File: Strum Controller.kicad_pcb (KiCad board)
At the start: 2 copper layers, 18 parts, among them J1 USB_C_Receptacle_USB2.0, U1 RP2040, U2 NCP1117-3.3_SOT223

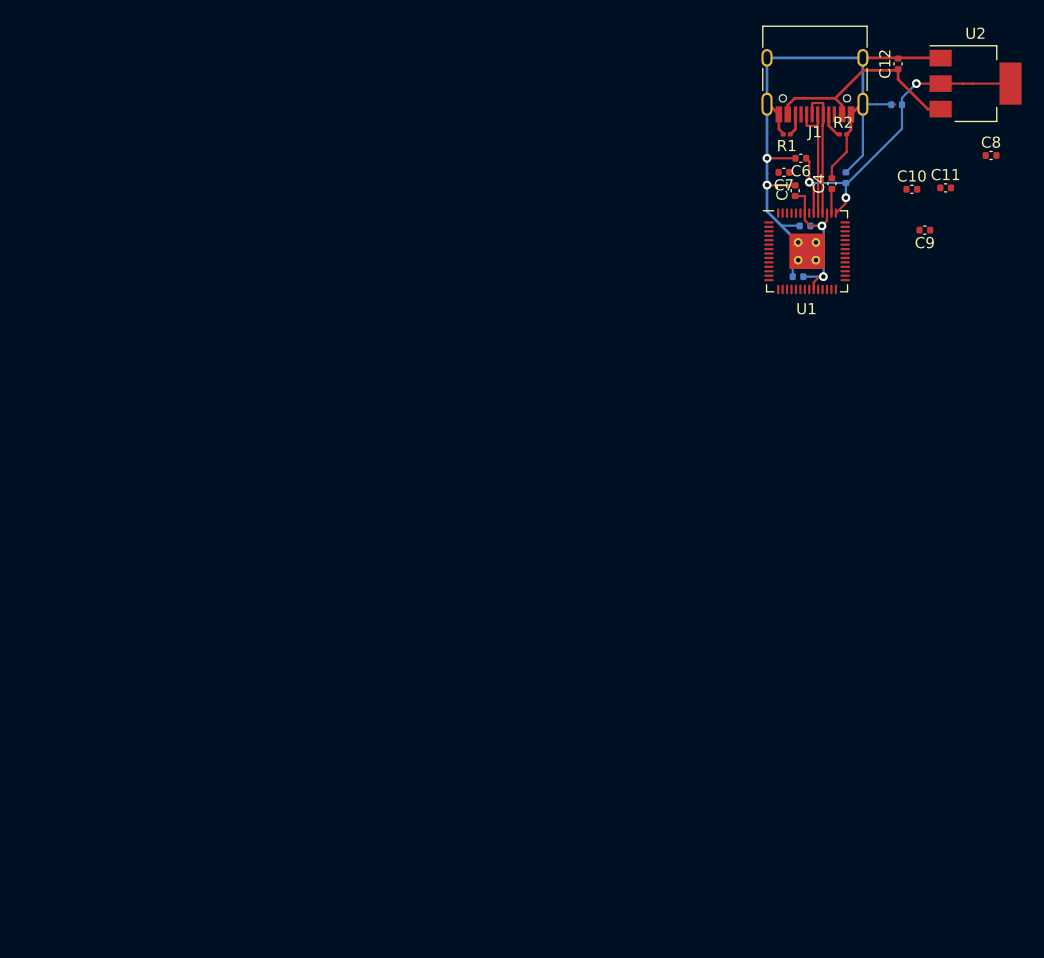
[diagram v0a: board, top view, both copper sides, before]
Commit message: Restart design using modified RP2040 minimal design from RasPi Foundation
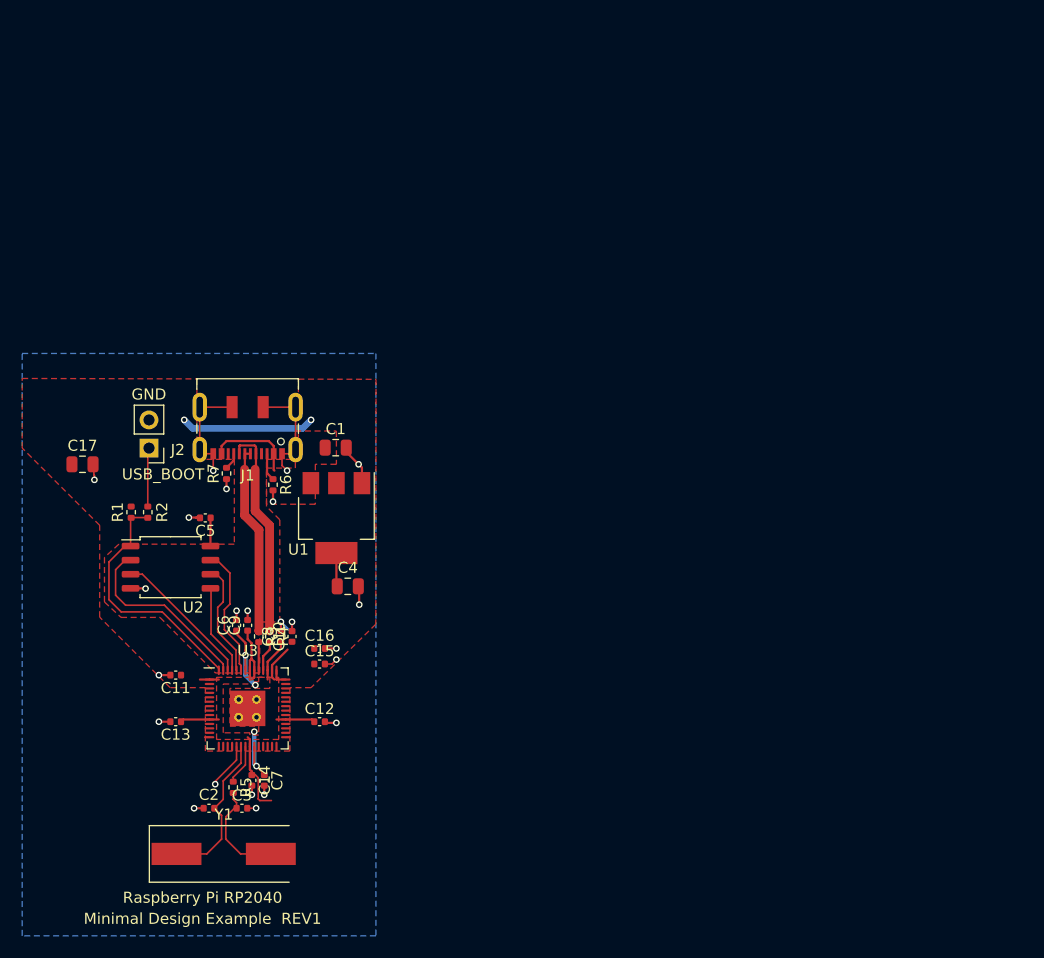
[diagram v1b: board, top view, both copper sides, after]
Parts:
- added C14: 100n, Capacitor_SMD:C_0402_1005Metric, F.Cu at (100.4, 106.5)
- added C15: 100n, Capacitor_SMD:C_0402_1005Metric, F.Cu at (106.5, 96.0)
- added C16: 100n, Capacitor_SMD:C_0402_1005Metric, F.Cu at (106.5, 94.6)
- added C17: 10u, Capacitor_SMD:C_0805_2012Metric, F.Cu at (85.1, 78.0)
- added J2: Conn_01x02, Connector_PinHeader_2.54mm:PinHeader_1x02_P2.54mm_Vertical, F.Cu at (91.1, 76.5)
- added R3: 27, Resistor_SMD:R_0402_1005Metric, F.Cu at (101.0, 93.5)
- added R4: 27, Resistor_SMD:R_0402_1005Metric, F.Cu at (102.0, 93.5)
- added R5: 1k, Resistor_SMD:R_0402_1005Metric, F.Cu at (98.7, 107.1)
- added R6: 5k1, Resistor_SMD:R_0402_1005Metric, F.Cu at (102.3, 79.8)
- added R7: 5k1, Resistor_SMD:R_0402_1005Metric, F.Cu at (98.1, 78.8)
- added U3: RP2040, kicad-rp2040:RP2040_QFN-56_EP_7x7_Pitch0.4mm_ThermalVias, F.Cu at (100.0, 100.0)
- added Y1: ABLS-12.000MHZ-B4-T, Crystal:Crystal_SMD_HC49-SD, F.Cu at (97.8, 113.1)
- C1, C4: value 100n -> 10u; footprint Capacitor_SMD:C_0402_1005Metric -> Capacitor_SMD:C_0805_2012Metric
- C10, C8: value 100n -> 1u
- C12: value 10u -> 100n
- C13: value 10u -> 100n; moved to F.Cu
- C2: value 100n -> 27p; moved to F.Cu
- C3: value 1u -> 27p; moved to F.Cu
- C5: value 1u -> 100n; moved to F.Cu
- J1: footprint Connector_USB:USB_C_Receptacle_HRO_TYPE-C-31-M-12 -> Connector_USB:USB_C_Receptacle_JAE_DX07S016JA1R1500
- R1: value 5k1 -> 1k; footprint Resistor_SMD:R_0201_0603Metric -> Resistor_SMD:R_0402_1005Metric
- R2: value 5k1 -> DNF; footprint Resistor_SMD:R_0201_0603Metric -> Resistor_SMD:R_0402_1005Metric
- U1: value RP2040 -> NCP1117-3.3_SOT223; footprint kicad-rp2040:RP2040_QFN-56_EP_7x7_Pitch0.4mm_ThermalVias -> Package_TO_SOT_SMD:SOT-223-3_TabPin2
- U2: value NCP1117-3.3_SOT223 -> W25Q128JVS; footprint Package_TO_SOT_SMD:SOT-223-3_TabPin2 -> Package_SO:SOIC-8_5.275x5.275mm_P1.27mm
- moved C13 85.5 mm to (93.5, 101.2)
- moved U2 84.6 mm to (93.0, 87.3)
- moved C11 82.1 mm to (93.5, 97.0), turned to 180 degrees
- moved C12 79.0 mm to (106.5, 101.2), turned to 0 degrees
- moved C8 77.3 mm to (103.0, 93.5), turned to 90 degrees
- moved C3 73.0 mm to (99.5, 109.0), turned to 0 degrees
- moved R2 72.6 mm to (89.5, 82.3), turned to -90 degrees
- moved C7 72.1 mm to (101.5, 106.5), turned to -90 degrees
- moved C2 71.5 mm to (96.5, 109.0)
- moved C9 70.7 mm to (100.0, 92.5), turned to 90 degrees
- moved C10 68.9 mm to (104.0, 93.5), turned to 90 degrees
- moved R1 66.9 mm to (91.0, 82.3), turned to 90 degrees
- moved C6 66.0 mm to (99.0, 92.5), turned to 90 degrees
- moved C5 65.4 mm to (96.2, 82.8), turned to 180 degrees
- moved J1 60.1 mm to (100.0, 74.0)
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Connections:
- C1 pad 1: +1V1 -> VBUS
- C12 pad 1: VBUS -> +3V3
- C2 pad 1: +1V1 -> /XIN
- C3 pad 1: +1V1 -> Net-(C3-Pad1)
- C6 pad 1: +3V3 -> +1V1
- C7 pad 1: +3V3 -> +1V1
- C8 pad 1: +3V3 -> +1V1
- J1 pad A6: /USB_+ -> /USB_D+
- J1 pad A7: /USB_- -> /USB_D-
- J1 pad B6: /USB_+ -> /USB_D+
- J1 pad B7: /USB_- -> /USB_D-
- R1 pad 1: Net-(J1-PadB5) -> /QSPI_SS
- R1 pad 2: GND -> /~{USB_BOOT}
- R2 pad 1: Net-(J1-PadA5) -> +3V3
- R2 pad 2: GND -> /QSPI_SS
- U1 pad 1: +3V3 -> GND
- U1 pad 2: unconnected-(U1-Pad2) -> +3V3
- U1 pad 3: unconnected-(U1-Pad3) -> VBUS
- U2 pad 1: GND -> /QSPI_SS
- U2 pad 2: +3V3 -> /QSPI_SD1
- U2 pad 3: VBUS -> /QSPI_SD2
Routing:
- net /QSPI_SS: track 0.00 -> 22.7 mm
- net /USB_D-: track 0.00 -> 19.5 mm
- net GND: track 67.0 -> 48.1 mm, vias 2 -> 23
- net /USB_D+: track 0.00 -> 17.0 mm
- net /QSPI_SD1: track 0.00 -> 16.8 mm
- net /XIN: track 0.00 -> 14.5 mm
- net /QSPI_SD2: track 0.00 -> 12.9 mm
- net /USB_-: track 11.9 -> 0.00 mm
- net /USB_+: track 11.9 -> 0.00 mm
- net +3V3: track 33.9 -> 45.8 mm, vias 3 -> 2
- net /QSPI_SD3: track 0.00 -> 11.8 mm
- net VBUS: track 19.7 -> 8.02 mm
- net /QSPI_SCLK: track 0.00 -> 10.4 mm
- net Net-(C3-Pad1): track 0.00 -> 9.69 mm
- net /QSPI_SD0: track 0.00 -> 8.20 mm
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- added copper zone on F.Cu, net +1V1
- added copper zone on F.Cu, net +3V3
- added copper zone on B.Cu, net GND
- added copper zone on F.Cu, net VBUS
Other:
- rule pad_to_mask_clearance: 0 -> 0.051
- board text added: "GND"
- board text added: "Minimal Design Example REV1"
- board text added: "Raspberry Pi RP2040"
- board text added: "USB_BOOT"

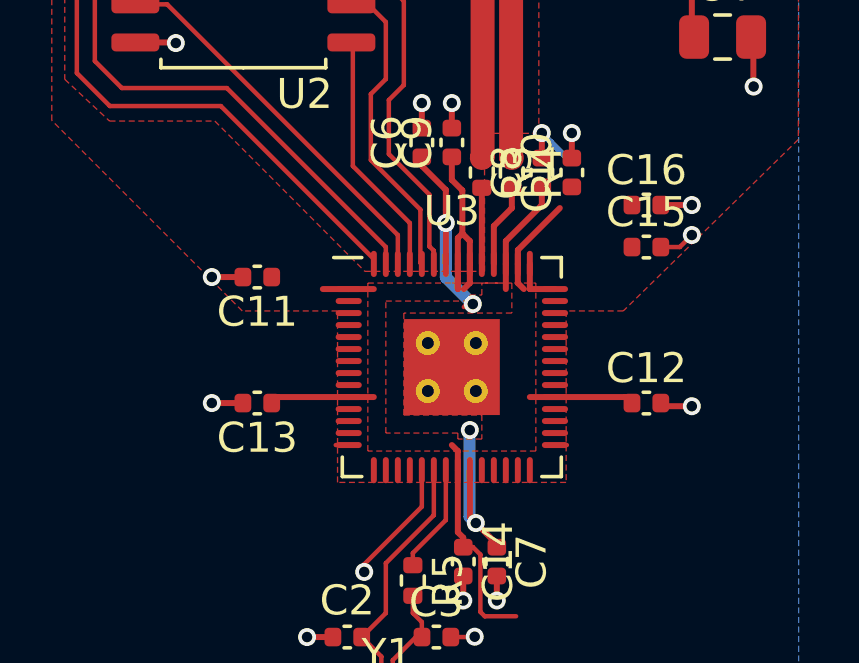
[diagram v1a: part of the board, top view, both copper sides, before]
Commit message: Move to proper RP2040 library
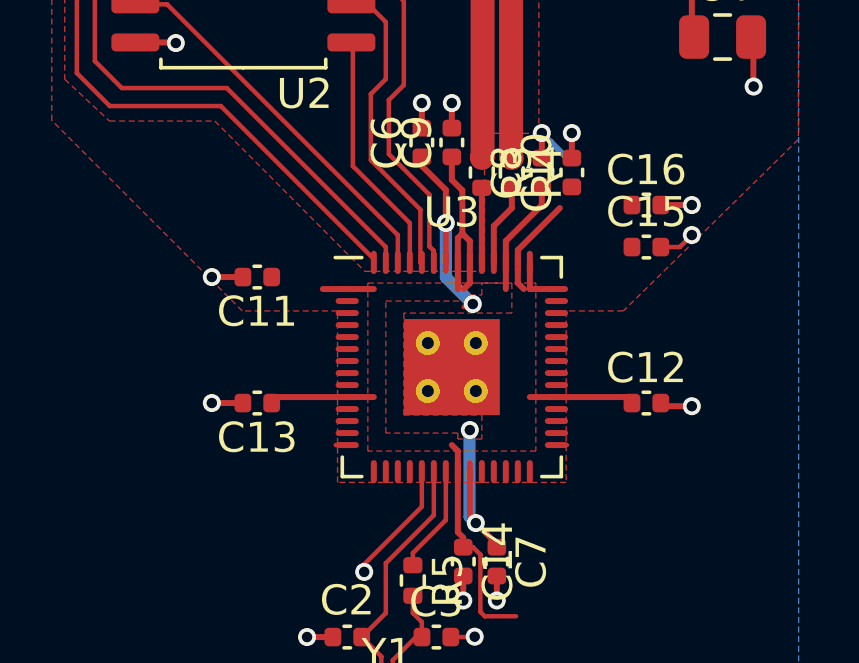
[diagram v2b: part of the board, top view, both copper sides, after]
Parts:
- U3: footprint kicad-rp2040:RP2040_QFN-56_EP_7x7_Pitch0.4mm_ThermalVias -> kicad-lib-rp2040:QFN-56_EP_7x7_Pitch0.4mm_ThermalVias
